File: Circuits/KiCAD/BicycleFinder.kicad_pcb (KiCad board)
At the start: 2 copper layers, 76.4 x 40.2 mm, 9 parts, among them P1 CONN_7, SW1 SW_PUSH, U1 LITE_LITE

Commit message: Fixed: Miss-connected GND line.
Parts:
- moved SW1 18.7 mm to (55.6, 40.9)
- moved P1 18.7 mm to (67.7, 27.6)
- moved BT1 18.7 mm to (79.8, 42.2)
- moved C1 18.7 mm to (32.8, 37.7)
- moved D1 18.7 mm to (36.6, 53.0), turned to 270 degrees
- moved R1 18.7 mm to (46.7, 28.8)
- moved R2 18.7 mm to (42.9, 49.1)
- moved U1 18.7 mm to (86.1, 35.2)
- moved PBPS-85 18.7 mm to (54.4, 40.9)
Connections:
- net N-0000016 renamed /PRG
- net N-0000018 renamed /M1
- net N-0000019 renamed /TX
- net N-0000029 renamed /RX
- net N-0000030 renamed /DI1
- net N-0000033 renamed /DO4
- net N-0000034 renamed /Vcc
- P1 pad 2: N-0000028 -> /RST
- P1 pad 6: N-0000028 -> GND
- U1 pad 21: N-0000028 -> /RST
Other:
- outline, holes or cut-outs redrawn
- net class power added: clearance 0.254, trace_width 0.508, via_dia 0.889, via_drill 0.635

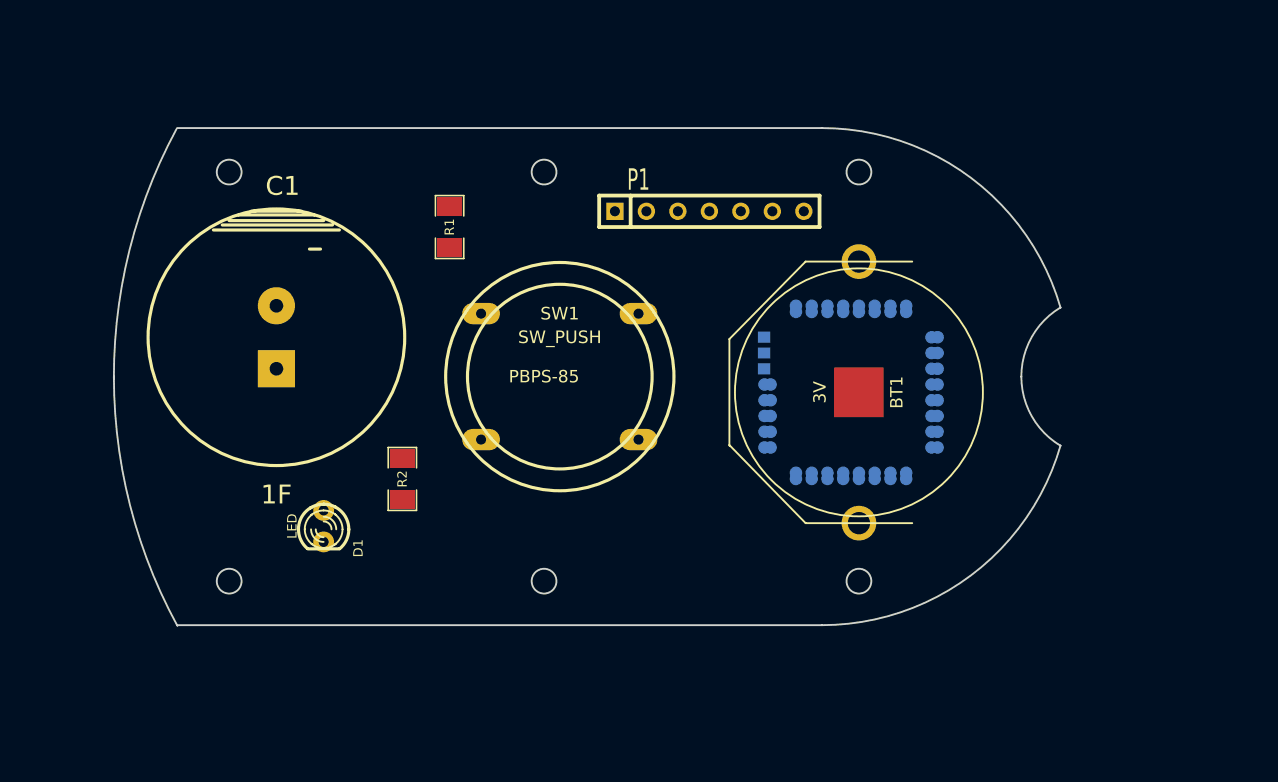
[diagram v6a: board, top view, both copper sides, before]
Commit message: Don't use arc in Edge.Cut layer.
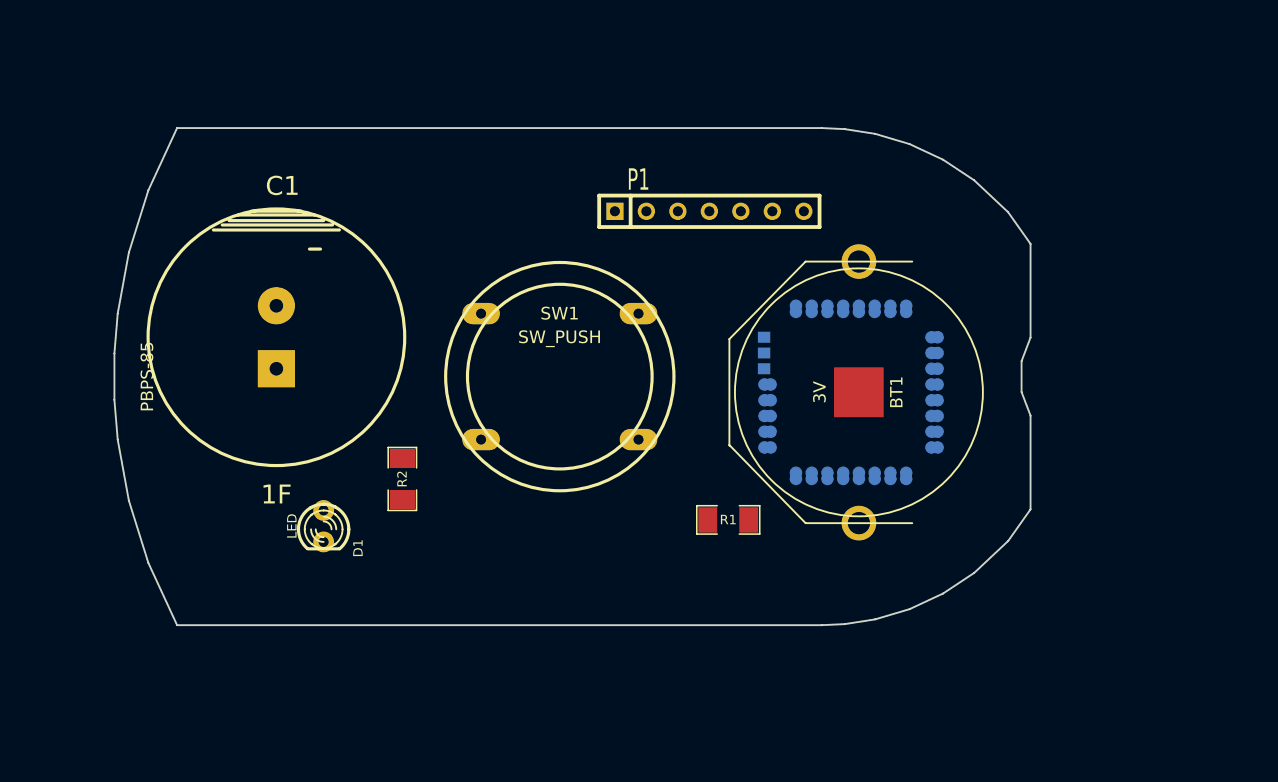
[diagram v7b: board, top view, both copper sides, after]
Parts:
- PBPS-85: footprint PS-85 -> PBPS-85-noNTH
- moved R1 32.6 mm to (69.2, 52.5), turned to 180 degrees
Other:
- board size 76.4 x 40.2 mm -> 73.9 x 40.1 mm
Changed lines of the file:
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@@
     (links 20)
     (no_connects 20)
-    (area 19.05 20.32 99.695 61.595)
+    (area 19.326999 20.514999 99.685001 61.328059)
     (thickness 1.6)
     (drawings 0)
@@
   )
   (module SM1206 (layer F.Cu)
-    (at 46.736 28.829 90)
+    (at 69.215 52.451 180)
     (attr smd)
-    (fp_text reference R1 (at 0 0 90) (layer F.SilkS)
+    (fp_text reference R1 (at 0 0 180) (layer F.SilkS)
       (effects (font (size 0.762 0.762) (thickness 0.127)))
     )
-    (fp_text value 750 (at 0 0 90) (layer F.SilkS) hide
+    (fp_text value 750 (at 0 0 180) (layer F.SilkS) hide
       (effects (font (size 0.762 0.762) (thickness 0.127)))
     )
@@
     (fp_line (start 2.54 1.143) (end 0.889 1.143) (layer F.SilkS) (width 0.127))
     (fp_line (start -0.889 -1.143) (end -2.54 -1.143) (layer F.SilkS) (width 0.127))
-    (pad 1 smd rect (at -1.651 0 90) (size 1.524 2.032)
+    (pad 1 smd rect (at -1.651 0 180) (size 1.524 2.032)
       (layers F.Cu F.Paste F.Mask)
       (net 1 /3V)
     )
-    (pad 2 smd rect (at 1.651 0 90) (size 1.524 2.032)
+    (pad 2 smd rect (at 1.651 0 180) (size 1.524 2.032)
       (layers F.Cu F.Paste F.Mask)
       (net 9 /Vcc)
@@
     )
   )
-  (module PS-85 (layer F.Cu)
+  (module PBPS-85-noNTH (layer F.Cu)
     (at 54.356 40.894)
-    (fp_text reference PBPS-85 (at 0 0) (layer F.SilkS)
+    (fp_text reference PBPS-85 (at -32 0 90) (layer F.SilkS)
       (effects (font (size 1 1) (thickness 0.15)))
     )
@@
       (effects (font (size 1.524 1.524) (thickness 0.000001)))
     )
-    (fp_circle (center 25.4 -16.5) (end 25.4 -15.5) (layer Edge.Cuts) (width 0.15))
-    (fp_circle (center 25.4 16.5) (end 25.4 15.5) (layer Edge.Cuts) (width 0.15))
-    (fp_circle (center -25.4 16.5) (end -25.4 15.5) (layer Edge.Cuts) (width 0.15))
-    (fp_circle (center -25.4 -16.5) (end -25.4 -15.5) (layer Edge.Cuts) (width 0.15))
-    (fp_circle (center 0 16.5) (end 0 17.5) (layer Edge.Cuts) (width 0.15))
-    (fp_circle (center 0 -16.5) (end 0.05 -17.5) (layer Edge.Cuts) (width 0.15))
-    (fp_arc (start 7.3 0) (end -34.7 0) (angle -28.6) (layer Edge.Cuts) (width 0.15))
-    (fp_arc (start 7.3 0) (end -34.7 0.15) (angle 28.6) (layer Edge.Cuts) (width 0.15))
-    (fp_arc (start 45 0) (end 38.5 0) (angle 59.1) (layer Edge.Cuts) (width 0.15))
-    (fp_arc (start 45 0) (end 38.5 0) (angle -59.1) (layer Edge.Cuts) (width 0.15))
-    (fp_arc (start 22.4 0) (end 22.4 20.05) (angle -73.9) (layer Edge.Cuts) (width 0.15))
-    (fp_arc (start 22.4 0) (end 22.4 -20.05) (angle 73.9) (layer Edge.Cuts) (width 0.15))
     (fp_line (start -29.6 -20.05) (end 22.4 -20.05) (layer Edge.Cuts) (width 0.15))
+    (fp_line (start -29.6 -20.05) (end -31.9151 -15.0368) (layer Edge.Cuts) (width 0.15))
+    (fp_line (start -31.9151 -15.0368) (end -33.4899 -10.0076) (layer Edge.Cuts) (width 0.15))
+    (fp_line (start -33.4899 -10.0076) (end -34.3916 -5.08) (layer Edge.Cuts) (width 0.15))
+    (fp_line (start -34.3916 -5.08) (end -34.6583 -1.8669) (layer Edge.Cuts) (width 0.15))
+    (fp_line (start -34.6583 -1.8669) (end -34.6583 1.8669) (layer Edge.Cuts) (width 0.15))
+    (fp_line (start -34.6583 1.8669) (end -34.3916 5.08) (layer Edge.Cuts) (width 0.15))
+    (fp_line (start -33.4899 10.0076) (end -34.3916 5.08) (layer Edge.Cuts) (width 0.15))
+    (fp_line (start -31.9151 15.0368) (end -33.4899 10.0076) (layer Edge.Cuts) (width 0.15))
+    (fp_line (start -29.6 20.05) (end -31.9151 15.0368) (layer Edge.Cuts) (width 0.15))
     (fp_line (start -29.6 20.05) (end 22.4 20.05) (layer Edge.Cuts) (width 0.15))
+    (fp_line (start 22.4 20.05) (end 24.257 19.9644) (layer Edge.Cuts) (width 0.15))
+    (fp_line (start 24.257 19.9644) (end 26.7081 19.5834) (layer Edge.Cuts) (width 0.15))
+    (fp_line (start 26.7081 19.5834) (end 29.4894 18.7579) (layer Edge.Cuts) (width 0.15))
+    (fp_line (start 29.4894 18.7579) (end 32.1818 17.5006) (layer Edge.Cuts) (width 0.15))
+    (fp_line (start 32.1818 17.5006) (end 34.6964 15.8369) (layer Edge.Cuts) (width 0.15))
+    (fp_line (start 34.6964 15.8369) (end 37.4396 13.2588) (layer Edge.Cuts) (width 0.15))
+    (fp_line (start 37.4396 13.2588) (end 39.243 10.7061) (layer Edge.Cuts) (width 0.15))
+    (fp_line (start 39.243 3.1496) (end 39.243 10.7061) (layer Edge.Cuts) (width 0.15))
+    (fp_line (start 38.5191 1.2446) (end 39.243 3.1496) (layer Edge.Cuts) (width 0.15))
+    (fp_line (start 38.5191 -1.2446) (end 38.5191 1.2446) (layer Edge.Cuts) (width 0.15))
+    (fp_line (start 38.5191 -1.2446) (end 39.243 -3.1496) (layer Edge.Cuts) (width 0.15))
+    (fp_line (start 39.243 -3.1496) (end 39.243 -10.7061) (layer Edge.Cuts) (width 0.15))
+    (fp_line (start 37.4396 -13.2588) (end 39.243 -10.7061) (layer Edge.Cuts) (width 0.15))
+    (fp_line (start 34.6964 -15.8369) (end 37.4396 -13.2588) (layer Edge.Cuts) (width 0.15))
+    (fp_line (start 32.1818 -17.5006) (end 34.6964 -15.8369) (layer Edge.Cuts) (width 0.15))
+    (fp_line (start 29.4894 -18.7579) (end 32.1818 -17.5006) (layer Edge.Cuts) (width 0.15))
+    (fp_line (start 26.7081 -19.5834) (end 29.4894 -18.7579) (layer Edge.Cuts) (width 0.15))
+    (fp_line (start 24.257 -19.9644) (end 26.7081 -19.5834) (layer Edge.Cuts) (width 0.15))
+    (fp_line (start 22.4 -20.05) (end 24.257 -19.9644) (layer Edge.Cuts) (width 0.15))
+  )
+  (zone (net 0) (net_name "") (layer B.Cu) (hatch edge 0.508)
+    (connect_pads (clearance 0.508))
+    (min_thickness 0.254)
+    (keepout (tracks not_allowed) (vias not_allowed) (copperpour allowed))
+    (fill (arc_segments 16) (thermal_gap 0.508) (thermal_bridge_width 0.508))
+    (polygon
+      (pts
+        (xy 84.963 48.006) (xy 73.279 48.006) (xy 73.279 41.275) (xy 72.771 40.894) (xy 72.771 36.322)
+        (xy 84.963 36.322)
+      )
+    )
   )
 )

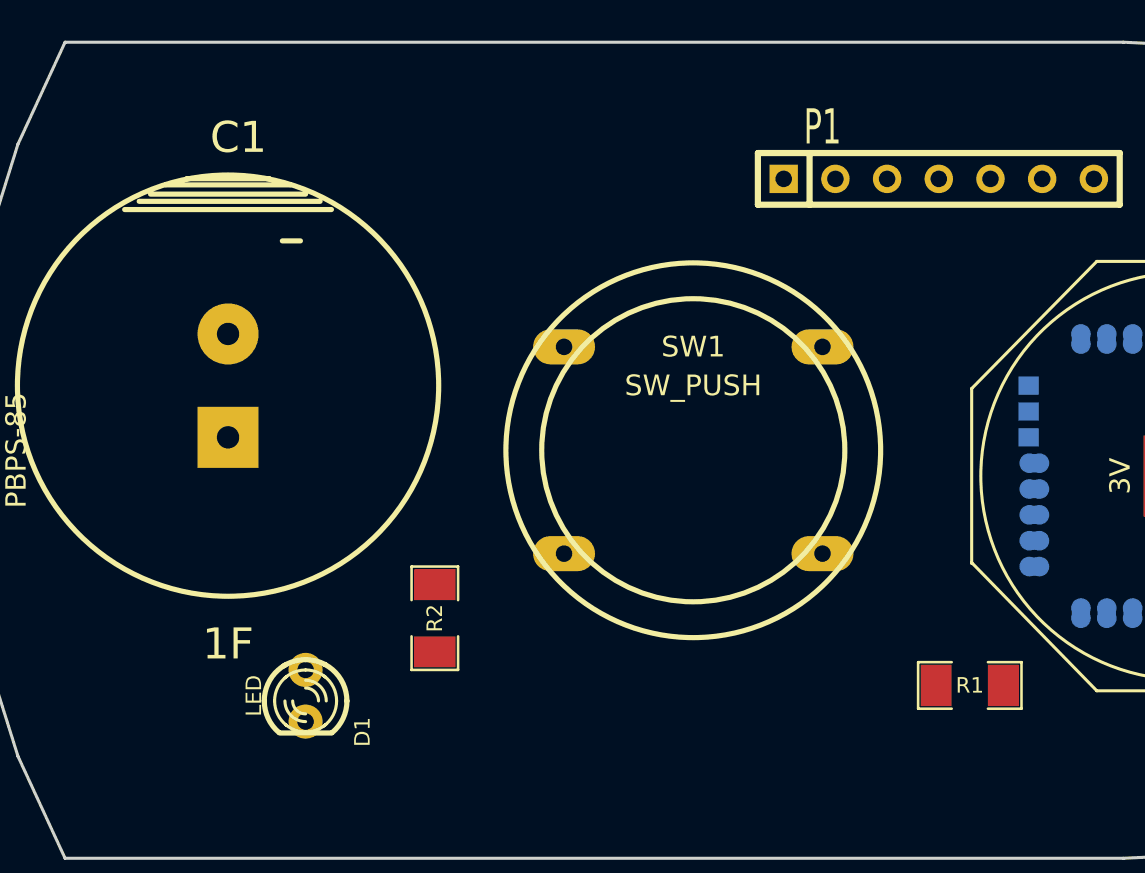
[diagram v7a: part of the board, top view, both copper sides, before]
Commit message: Added a diode array.
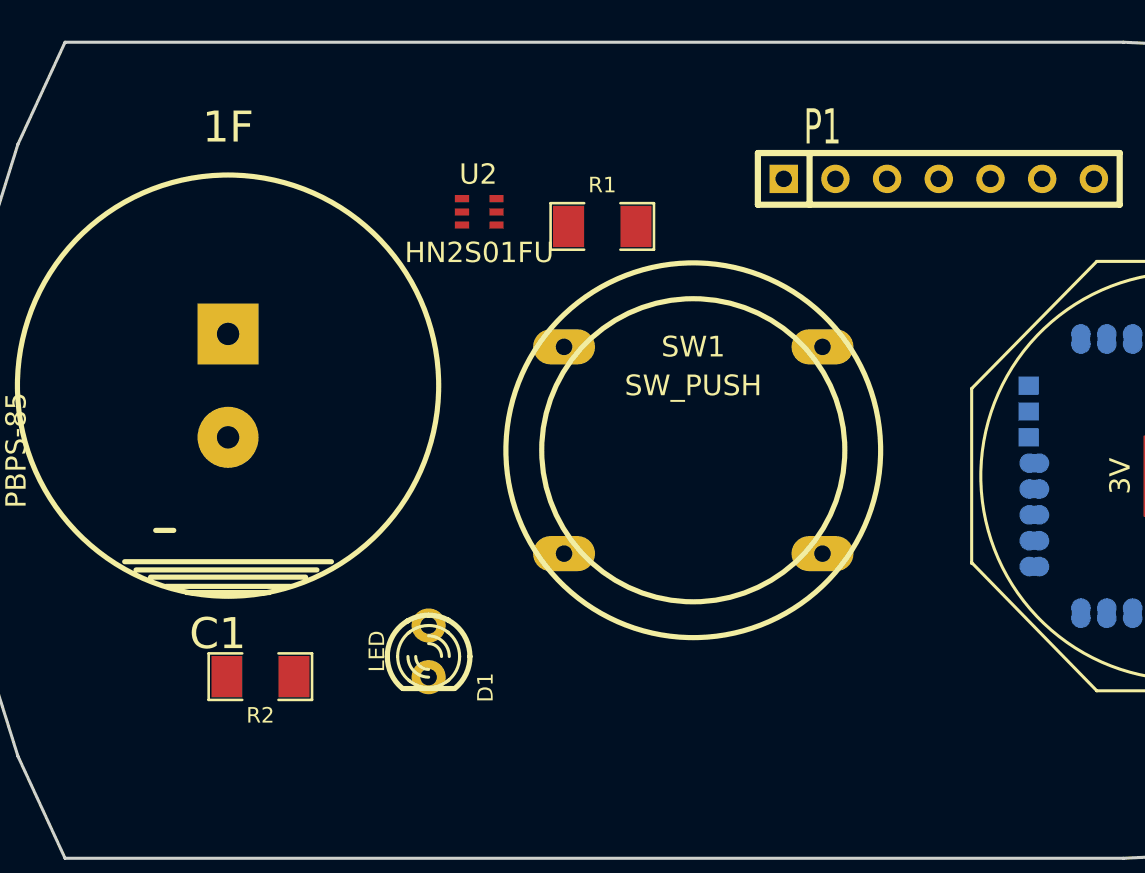
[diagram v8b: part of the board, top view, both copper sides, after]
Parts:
- added U2: HN2S01FU, HN2S01FU, F.Cu at (45.1, 29.2)
- moved R1 28.9 mm to (51.2, 29.9)
- moved R2 9.04 mm to (34.4, 52.0), turned to 180 degrees
- moved D1 6.43 mm to (42.6, 50.8)
- turned C1 to 180 degrees
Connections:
- net /DO4 renamed /K
- net N-0000031 renamed /A
- P1 pad 1: /Vcc -> /DC3V
- R1 pad 2: /Vcc -> /CHG
